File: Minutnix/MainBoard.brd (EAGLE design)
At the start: 222.3 x 73.3 mm, 121 parts, among them IC3 TP4056, IC7 FT232RL, Q4 32.768kHz, X1 FH12-12S-0.5S_THINNER, X2 JST-XH-03-PIN-LONG-PAD, X4 JST-XH-03-PIN-LONG-PAD

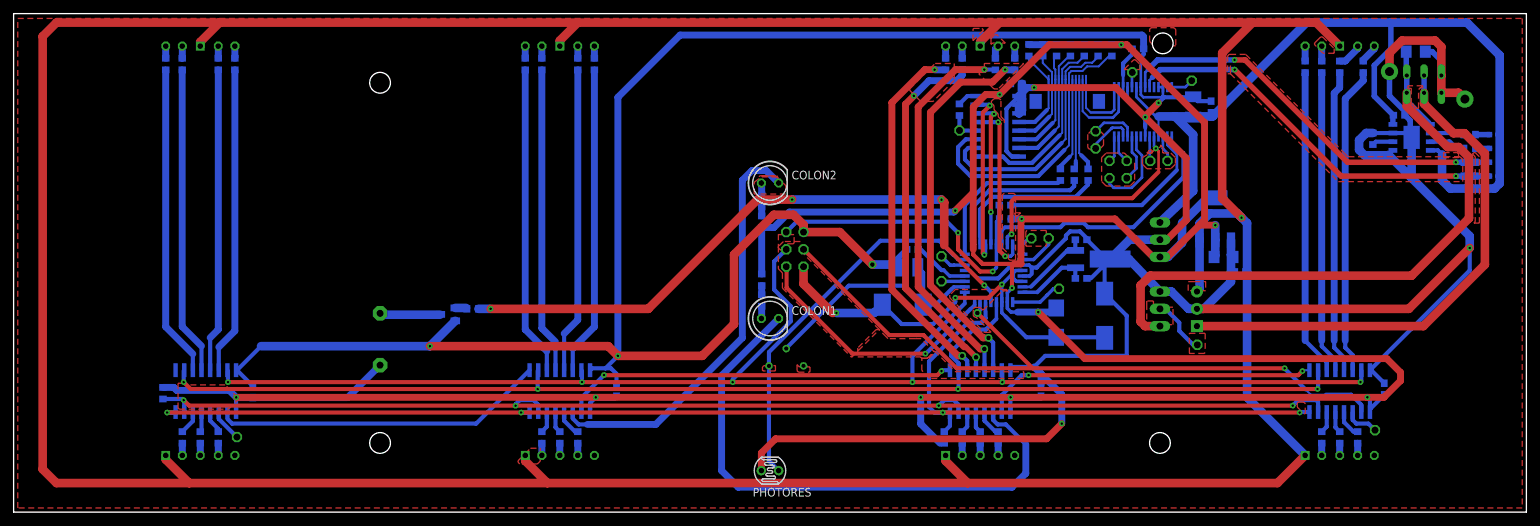
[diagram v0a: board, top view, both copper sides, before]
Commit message: Main board gnd bottom pool
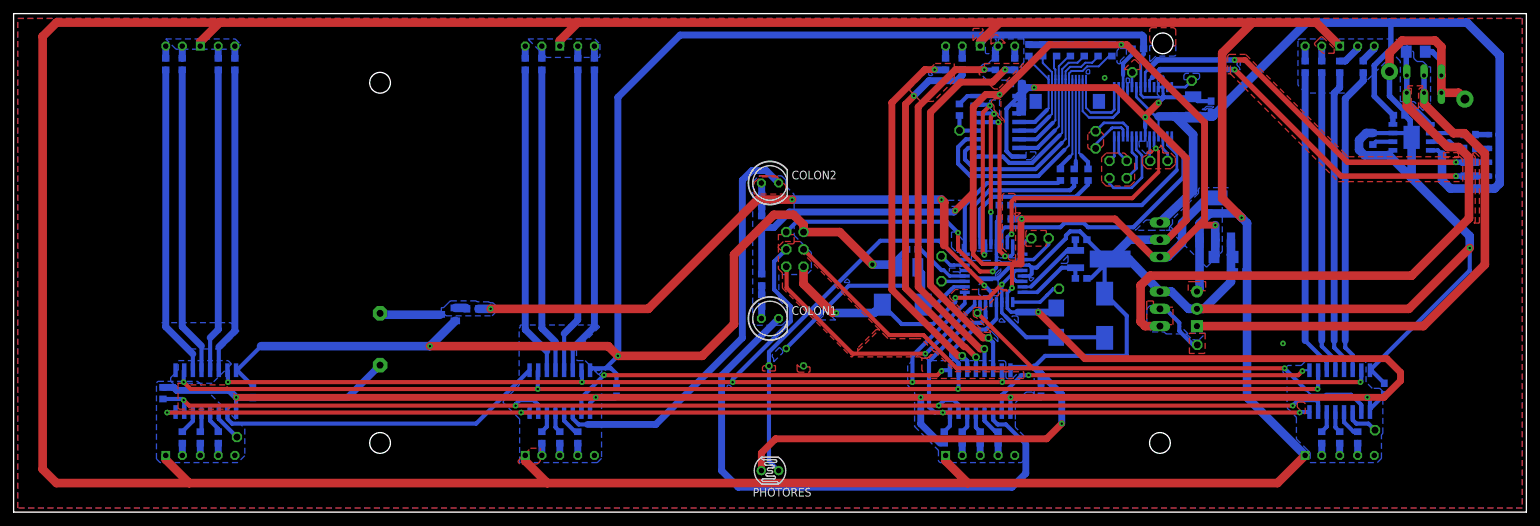
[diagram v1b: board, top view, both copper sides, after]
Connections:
- net GND: now also X1.CASE1, X1.CASE2
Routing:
- net GND: vias 8 -> 10
- added copper zone on layer 16, net GND

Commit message: Many final changes
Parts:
- removed IC2: (no value), v-reg-2:SOT223
- removed IC3: TP4056, TP4056:SOP-8
- removed Q4: 32.768kHz, crystal_clock:CRYSTAL-SMD-2X6-CYL
- removed R57: (no value), rcl:RTRIM3296Y
- removed SG1: F/HGP, buzzer:F/HGP
- removed X2: JST-XH-03-PIN-LONG-PAD, Rembrandt Electronics - JST XH Connectors v1-0:JST-XH-03-PACKAGE-LONG-PAD
- added BATTERY_CON: JST-XH-03-PIN-LONG-PAD, Rembrandt Electronics - JST XH Connectors v1-0:JST-XH-03-PACKAGE-LONG-PAD
- added BUZZER: F/HGP, Mybuzzer:F/HGP
- added CHARGER: TP4056, TP4056:SOP-8
- added LDO_5V: (no value), v-reg-2:SOT223
- added POTENTIOMETER: (no value), Myrcl:RTRIM3296Y
- added QUARTZ: 32.768kHz, crystal_clock:CRYSTAL-SMD-2X6-CYL
- COLON1, COLON2: device led:LED5MM -> Myled:LED5MM
- EXPANDER: value PCF8574AT -> PCF8574T; device i2c:SO16 -> micro-philips:SO16W
- PHOTORES: device photo-elements:VT900 -> Myphoto-elements:VT900
- SPI_JUMPERS: device con-lstb:MA03-2 -> Mycon-lstb:MA03-2
- moved JP6 3.86 mm to (135.1, 56.1)
- moved R61 3.86 mm to (135.1, 59.1)
- moved R15 2.30 mm to (188.2, 63.8)
- moved R16 2.30 mm to (190.6, 63.8)
- moved R20 2.30 mm to (196.7, 63.8)
- moved R21 2.30 mm to (193.2, 63.8)
- moved C2 2.24 mm to (203.6, 56.1)
- moved CHRG_LED 2.24 mm to (217.6, 51.2)
- moved R39 2.24 mm to (214.0, 51.2)
- moved R40 2.24 mm to (214.0, 53.2)
- moved R48 2.24 mm to (199.7, 52.6)
- moved R65 2.24 mm to (214.0, 49.2)
- moved R66 2.24 mm to (214.0, 47.1)
- moved RXLED 2.24 mm to (217.6, 49.2)
- moved STDBY_LED 2.24 mm to (217.6, 53.2)
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- renumbered IC7 to FTDI, Q2 to NPN_AMP, SHOTTKYDIODE3 to SHOTTKY, X1 to FFC_CON, X4 to POWER_CON
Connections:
- net +5V: now also CHARGER.4, CHARGER.8; no longer IC3.4, IC3.8
- net AVCC: now also POTENTIOMETER.1; no longer R57.2
- net BATTERY+: now also BATTERY_CON.1, CHARGER.5; no longer IC3.5, X2.1
- net BATTERY_S: now also BATTERY_CON.2; no longer X2.2
- net COUNTER: now also EXPANDER.9, FFC_CON.8, R42.2; no longer EXPANDER.6, FFC_CON.10, R44.2
- net GND: now also BATTERY_CON.3, CHARGER.1, CHARGER.3, CHARGER.ETP, LDO_5V.1, QUARTZ.SHEILD; no longer FFC_CON.CASE1, FFC_CON.CASE2, IC2.1, IC3.1, IC3.3, IC3.ETP, Q4.SHEILD, X2.3
- net LIGHT_SENS: now also POTENTIOMETER.2; no longer R57.3
- net N$52: now also CHARGER.7; no longer IC3.7
- net N$53: now also CHARGER.6; no longer IC3.6
- net N$66: now also BUZZER.2; no longer SG1.2
- net N$82: now also CHARGER.2; no longer IC3.2
- net PLAY/PAUSE: now also EXPANDER.4, FFC_CON.12, R46.2; no longer EXPANDER.5, FFC_CON.11, R45.2
- net STOP/RESET: now also EXPANDER.5, FFC_CON.11, R45.2; no longer EXPANDER.4, FFC_CON.12, R46.2
- net VCC: now also BUZZER.1, LDO_5V.2, LDO_5V.4; no longer IC2.2, IC2.4, SG1.1
- net VDD: now also LDO_5V.3; no longer IC2.3
- net VOLUME: now also EXPANDER.6, FFC_CON.10, R44.2; no longer EXPANDER.9, FFC_CON.8, R42.2
- net XTAL1: now also QUARTZ.X2; no longer Q4.X2
- net XTAL2: now also QUARTZ.X1; no longer Q4.X1
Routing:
- net GND: track 668.0 -> 296.4 mm, vias 10 -> 13
- net VDD: track 562.5 -> 514.6 mm
- net COUNTER: track 16.4 -> 31.2 mm
- net VOLUME: track 28.1 -> 16.5 mm
- net BATTERY+: track 96.1 -> 104.8 mm
- net MS_B: track 57.2 -> 63.1 mm
- net N$27: track 8.33 -> 4.74 mm
- net ENC_A: track 36.2 -> 39.5 mm
- net ENC_B: track 42.6 -> 45.7 mm
- net EXP_INT: track 25.9 -> 28.9 mm
- net LIGHT_SENS: track 54.7 -> 57.2 mm
- net N$42: track 2.20 -> 4.59 mm
- net N$48: track 3.77 -> 6.11 mm
- net N$47: track 2.87 -> 5.20 mm
- net N$41: track 2.20 -> 4.52 mm
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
